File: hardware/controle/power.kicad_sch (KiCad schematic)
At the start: 15 parts, among them J1 Barrel_Jack, U3 TPS54228

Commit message: Adjust some references and availability
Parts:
- C10: P/N C0603C100J5GACTU -> C0603C100J5ACTU
- C9: footprint Capacitor_SMD:C_0805_2012Metric_Pad1.18x1.45mm_HandSolder -> Capacitor_SMD:C_0603_1608Metric_Pad1.08x0.95mm_HandSolder; P/N GRM21BR71E105KA99L -> CGA3E1X7R1V105K080AC (stock)
- R3: footprint Resistor_SMD:R_1206_3216Metric_Pad1.30x1.75mm_HandSolder -> Resistor_SMD:R_0805_2012Metric_Pad1.20x1.40mm_HandSolder; P/N (none) -> stock
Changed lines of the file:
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@@
 			)
 		)
-		(property "Footprint" "Capacitor_SMD:C_0805_2012Metric_Pad1.18x1.45mm_HandSolder"
+		(property "Footprint" "Capacitor_SMD:C_0603_1608Metric_Pad1.08x0.95mm_HandSolder"
 			(at 92.71 92.71 0)
 			(effects
@@
 			)
 		)
-		(property "P/N" "GRM21BR71E105KA99L"
+		(property "P/N" "CGA3E1X7R1V105K080AC (stock)"
 			(at 92.71 92.71 0)
 			(effects
@@
 			)
 		)
-		(property "Footprint" "Resistor_SMD:R_1206_3216Metric_Pad1.30x1.75mm_HandSolder"
+		(property "Footprint" "Resistor_SMD:R_0805_2012Metric_Pad1.20x1.40mm_HandSolder"
 			(at 92.71 71.12 0)
 			(effects
@@
 		(property "Description" ""
 			(at 92.71 71.12 0)
+			(effects
+				(font
+					(size 1.27 1.27)
+				)
+				(hide yes)
+			)
+		)
+		(property "P/N" "stock"
+			(at 92.71 71.12 90)
 			(effects
 				(font
@@
 			)
 		)
-		(property "P/N" "C0603C100J5GACTU"
+		(property "P/N" "C0603C100J5ACTU"
 			(at 148.59 92.71 0)
 			(effects

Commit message: controle: - pass ERC - adjust some components and connections - place components on board
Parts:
- +5V1: symbol centrale-rescue:Conn_01x02_Male-Connector -> Connector_Generic:Conn_01x02
- L1: symbol centrale-rescue:INDUCTOR-pspice -> Device:L_Small
- R5: footprint Resistor_SMD:R_1206_3216Metric_Pad1.30x1.75mm_HandSolder -> Resistor_SMD:R_0805_2012Metric_Pad1.20x1.40mm_HandSolder
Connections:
- net GND: now also J1.3
- no-connect marks 2 -> 0
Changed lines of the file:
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@@
+	)
+	(junction
+		(at 58.42 67.31)
+		(diameter 0)
+		(color 0 0 0 0)
 	)
 	(junction
@@
 		(color 0 0 0 0)
 	)
-	(no_connect
-		(at 194.31 161.29)
-	)
-	(no_connect
-		(at 58.42 64.77)
-	)
 	(wire
 		(pts
@@
 	(wire
 		(pts
-			(xy 149.86 82.55) (xy 152.4 82.55)
+			(xy 149.86 82.55) (xy 156.21 82.55)
 		)
 		(stroke
@@
 	(wire
 		(pts
+			(xy 161.29 82.55) (xy 166.37 82.55)
+		)
+		(stroke
+			(width 0)
+			(type default)
+		)
+	)
+	(wire
+		(pts
 			(xy 118.11 100.33) (xy 118.11 102.87)
 		)
@@
 	(wire
 		(pts
+			(xy 58.42 64.77) (xy 58.42 67.31)
+		)
+		(stroke
+			(width 0)
+			(type default)
+		)
+	)
+	(wire
+		(pts
 			(xy 179.07 100.33) (xy 179.07 95.25)
 		)
@@
 		(pts
 			(xy 68.58 100.33) (xy 68.58 102.87)
-		)
-		(stroke
-			(width 0)
-			(type default)
-		)
-	)
-	(wire
-		(pts
-			(xy 166.37 82.55) (xy 165.1 82.55)
 		)
 		(stroke
@@
 			)
 		)
-		(property "Description" ""
+		(property "Description" "Switching Regulator"
 			(at 118.11 82.55 0)
 			(effects
@@
 			)
 		)
-		(property "Footprint" "Resistor_SMD:R_1206_3216Metric_Pad1.30x1.75mm_HandSolder"
+		(property "Footprint" "Resistor_SMD:R_0805_2012Metric_Pad1.20x1.40mm_HandSolder"
 			(at 144.78 96.52 0)
 			(effects
@@
 	)
 	(symbol
-		(lib_id "centrale-rescue:INDUCTOR-pspice")
-		(at 158.75 82.55 0)
+		(lib_id "Device:L_Small")
+		(at 158.75 82.55 90)
 		(unit 1)
 		(exclude_from_sim no)
@@
 		(dnp no)
 		(property "Reference" "L1"
-			(at 158.75 78.74 0)
+			(at 158.75 80.264 90)
 			(effects
 				(font
@@
 		)
 		(property "Value" "4.7µH"
-			(at 158.75 83.82 0)
+			(at 159.004 84.582 90)
 			(effects
 				(font
@@
 			)
 		)
-		(property "Datasheet" ""
+		(property "Datasheet" "~"
 			(at 158.75 82.55 0)
 			(effects
@@
 					(size 1.27 1.27)
 				)
-			)
-		)
-		(property "Description" ""
+				(hide yes)
+			)
+		)
+		(property "Description" "Inductor, small symbol"
 			(at 158.75 82.55 0)
 			(effects
@@
 	)
 	(symbol
-		(lib_id "centrale-rescue:GND2-power")
+		(lib_id "power:GND")
 		(at 118.11 102.87 0)
 		(unit 1)
@@
 			)
 		)
-		(property "Description" ""
+		(property "Description" "Power symbol creates a global label with name \"GND\" , ground"
 			(at 118.11 102.87 0)
 			(effects
@@
 	)
 	(symbol
-		(lib_id "centrale-rescue:GND2-power")
+		(lib_id "power:GND")
 		(at 130.81 64.77 90)
 		(unit 1)
@@
 			)
 		)
-		(property "Description" ""
+		(property "Description" "Power symbol creates a global label with name \"GND\" , ground"
 			(at 130.81 64.77 0)
 			(effects
@@
 	)
 	(symbol
-		(lib_id "centrale-rescue:Conn_01x02_Male-Connector")
-		(at 189.23 90.17 180)
+		(lib_id "Connector_Generic:Conn_01x02")
+		(at 189.23 90.17 0)
+		(mirror x)
 		(unit 1)
 		(exclude_from_sim no)
@@
 		)
 		(property "Value" "5V_LIME2"
-			(at 190.5 96.52 0)
+			(at 189.23 84.074 0)
 			(effects
 				(font
@@
 			)
 		)
-		(property "Datasheet" ""
+		(property "Datasheet" "~"
 			(at 189.23 90.17 0)
 			(effects
@@
 					(size 1.27 1.27)
 				)
-			)
-		)
-		(property "Description" ""
+				(hide yes)
+			)
+		)
+		(property "Description" "Generic connector, single row, 01x02, script generated (kicad-library-utils/schlib/autogen/connector/)"
 			(at 189.23 90.17 0)
 			(effects
@@
 	)
 	(symbol
-		(lib_id "centrale-rescue:+12V-power")
+		(lib_id "power:+12V")
 		(at 118.11 50.8 0)
 		(unit 1)
@@
 			)
 		)
-		(property "Description" ""
+		(property "Description" "Power symbol creates a global label with name \"+12V\""
 			(at 118.11 50.8 0)
 			(effects
+				(font
+					(size 1.27 1.27)
+				)
+				(hide yes)
+			)
+		)
+		(property "P/N" ""
+			(at 118.11 50.8 0)
+			(effects

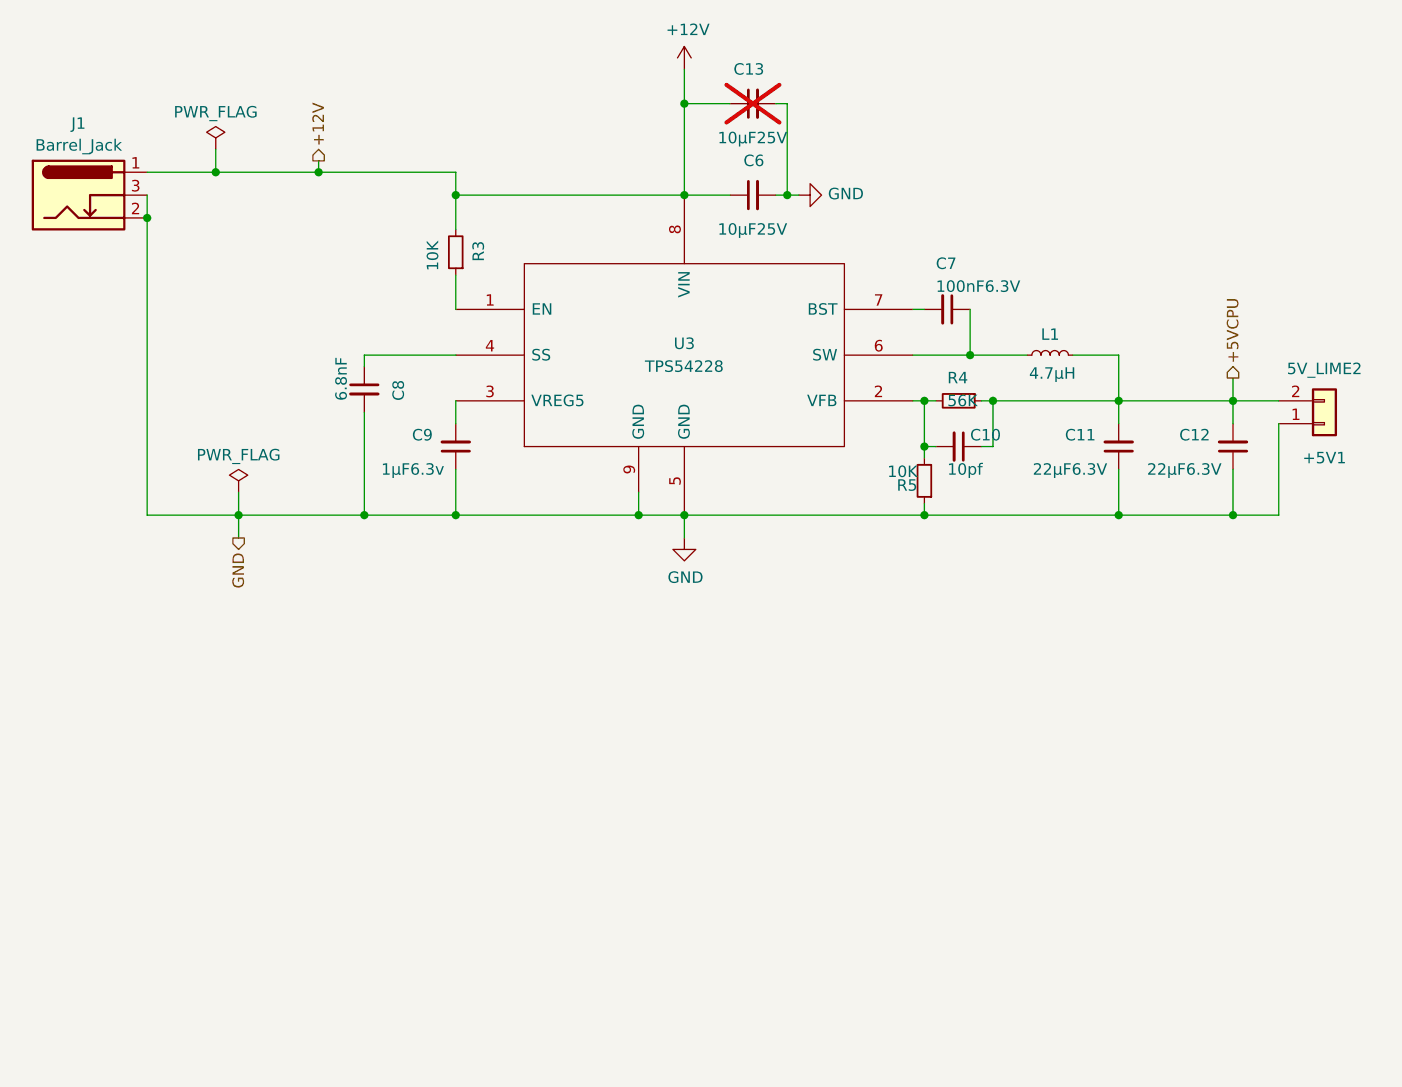
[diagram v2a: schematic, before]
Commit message: hardware/controle: control CPU power from pic18: - add a separate 3.3V power for pic18 - use the pic18 to start the tps54228
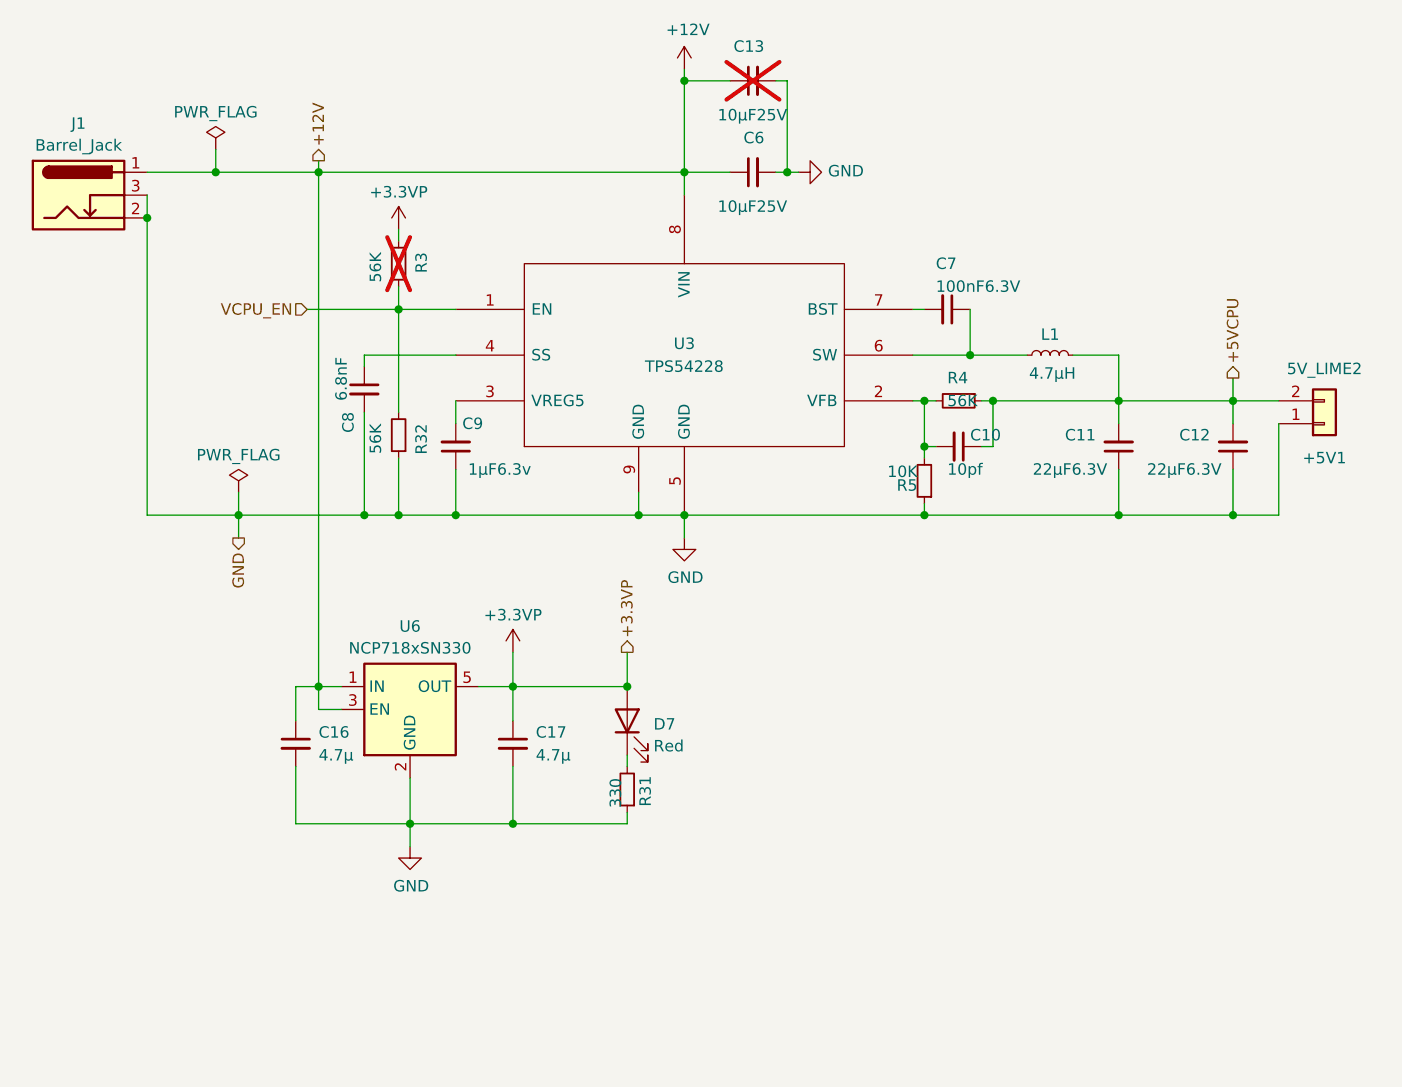
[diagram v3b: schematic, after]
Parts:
- added C16, C17: 4.7µ, Capacitor_SMD:C_0805_2012Metric_Pad1.18x1.45mm_HandSolder, symbol Device:C_Small
- added D7: Red, LED_SMD:LED_0805_2012Metric, symbol Device:LED
- added R31: 330, Resistor_SMD:R_0805_2012Metric_Pad1.20x1.40mm_HandSolder, symbol Device:R_Small
- added R32: 56K, Resistor_SMD:R_0805_2012Metric_Pad1.20x1.40mm_HandSolder, symbol Device:R_Small
- added U6: NCP718xSN330, Package_TO_SOT_SMD:SOT-23-5, symbol Regulator_Linear:NCP718xSN330
- R3: value 10K -> 56K; now not fitted; now left out of the parts list
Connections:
- net +12V: now also C16.1, U6.1 (IN), U6.3 (EN); no longer R3.2
- net GND: now also C16.2, C17.2, R31.1, R32.1, U6.2 (GND)
- net VCPU_EN: now reaches R3.1, U3.1 (EN)
- net VCPU_EN: now also R32.2
- new net: D7.1 (K), R31.2
- new net +3.3VP: C17.1, D7.2 (A), R3.2, U6.5 (OUT)
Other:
- moved on the sheet: C13, C6

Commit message: hardware/controle: route control CPU power from pic18
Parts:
- renumbered C9 to C10, C10 to C11, C11 to C12, C12 to C13, C16 to C14, C17 to C15, C13 to C6, C6 to C7, C7 to C8, C8 to C9, J1 to J9, R3 to R24, R4 to R25, R32 to R26, R5 to R27, R31 to R28, U3 to U4, U6 to U5
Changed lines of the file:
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@@
 		(on_board yes)
 		(dnp no)
-		(property "Reference" "#PWR022"
+		(property "Reference" "#PWR025"
 			(at 87.63 143.51 0)
 			(effects
@@
 			(project "controle"
 				(path "/41099c3f-2f7d-470d-b75f-9309d43eb2d2/523a32f9-902b-415b-ba1d-6227a5ae26a9"
-					(reference "#PWR022")
+					(reference "#PWR025")
 					(unit 1)
 				)
@@
 		(dnp no)
 		(fields_autoplaced yes)
-		(property "Reference" "#PWR01"
+		(property "Reference" "#PWR024"
 			(at 102.87 116.84 0)
 			(effects
@@
 			(project "controle"
 				(path "/41099c3f-2f7d-470d-b75f-9309d43eb2d2/523a32f9-902b-415b-ba1d-6227a5ae26a9"
-					(reference "#PWR01")
+					(reference "#PWR024")
 					(unit 1)
 				)
@@
 		(on_board yes)
 		(dnp no)
-		(property "Reference" "C9"
+		(property "Reference" "C10"
 			(at 95.758 90.17 0)
 			(effects
@@
 			(project "controle"
 				(path "/41099c3f-2f7d-470d-b75f-9309d43eb2d2/523a32f9-902b-415b-ba1d-6227a5ae26a9"
-					(reference "C9")
+					(reference "C10")
 					(unit 1)
 				)
@@
 		(on_board yes)
 		(dnp no)
-		(property "Reference" "C7"
+		(property "Reference" "C8"
 			(at 146.05 72.39 90)
 			(effects
@@
 			(project "controle"
 				(path "/41099c3f-2f7d-470d-b75f-9309d43eb2d2/523a32f9-902b-415b-ba1d-6227a5ae26a9"
-					(reference "C7")
+					(reference "C8")
 					(unit 1)
 				)
@@
 		(on_board yes)
 		(dnp yes)
-		(property "Reference" "C13"
+		(property "Reference" "C6"
 			(at 127 48.26 90)
 			(effects
@@
 			(project "controle"
 				(path "/41099c3f-2f7d-470d-b75f-9309d43eb2d2/523a32f9-902b-415b-ba1d-6227a5ae26a9"
-					(reference "C13")
+					(reference "C6")
 					(unit 1)
 				)
@@
 		(on_board yes)
 		(dnp no)
-		(property "Reference" "R4"
+		(property "Reference" "R25"
 			(at 147.32 85.09 90)
 			(effects
@@
 			(project "controle"
 				(path "/41099c3f-2f7d-470d-b75f-9309d43eb2d2/523a32f9-902b-415b-ba1d-6227a5ae26a9"
-					(reference "R4")
+					(reference "R25")
 					(unit 1)
 				)
@@
 		(on_board yes)
 		(dnp no)
-		(property "Reference" "C6"
+		(property "Reference" "C7"
 			(at 127 58.42 90)
 			(effects
@@
 			(project "controle"
 				(path "/41099c3f-2f7d-470d-b75f-9309d43eb2d2/523a32f9-902b-415b-ba1d-6227a5ae26a9"
-					(reference "C6")
+					(reference "C7")
 					(unit 1)
 				)
@@
 		(on_board yes)
 		(dnp no)
-		(property "Reference" "U3"
+		(property "Reference" "U4"
 			(at 118.11 81.28 0)
 			(effects
@@
 			(project "controle"
 				(path "/41099c3f-2f7d-470d-b75f-9309d43eb2d2/523a32f9-902b-415b-ba1d-6227a5ae26a9"
-					(reference "U3")
+					(reference "U4")
 					(unit 1)
 				)
@@
 		(on_board yes)
 		(dnp no)
-		(property "Reference" "R5"
+		(property "Reference" "R27"
 			(at 144.018 97.028 0)
 			(effects
@@
 			(project "controle"
 				(path "/41099c3f-2f7d-470d-b75f-9309d43eb2d2/523a32f9-902b-415b-ba1d-6227a5ae26a9"
-					(reference "R5")
+					(reference "R27")
 					(unit 1)
 				)
@@
 		(on_board yes)
 		(dnp no)
-		(property "Reference" "C12"
+		(property "Reference" "C13"
 			(at 176.53 91.44 0)
 			(effects
@@
 			(project "controle"
 				(path "/41099c3f-2f7d-470d-b75f-9309d43eb2d2/523a32f9-902b-415b-ba1d-6227a5ae26a9"
-					(reference "C12")
+					(reference "C13")
 					(unit 1)
 				)
@@
 		(dnp no)
 		(fields_autoplaced yes)
-		(property "Reference" "U6"
+		(property "Reference" "U5"
 			(at 87.63 112.6955 0)
 			(effects
@@
 			(project "controle"
 				(path "/41099c3f-2f7d-470d-b75f-9309d43eb2d2/523a32f9-902b-415b-ba1d-6227a5ae26a9"
-					(reference "U6")
+					(reference "U5")
 					(unit 1)
 				)
@@
 		(dnp no)
 		(fields_autoplaced yes)
-		(property "Reference" "#PWR035"
+		(property "Reference" "#PWR022"
 			(at 90.17 69.85 0)
 			(effects
@@
 			(project "controle"
 				(path "/41099c3f-2f7d-470d-b75f-9309d43eb2d2/523a32f9-902b-415b-ba1d-6227a5ae26a9"
-					(reference "#PWR035")
+					(reference "#PWR022")
 					(unit 1)
 				)
@@
 		(dnp no)
 		(fields_autoplaced yes)
-		(property "Reference" "C16"
+		(property "Reference" "C14"
 			(at 77.47 124.4662 0)
 			(effects
@@
 			(project "controle"
 				(path "/41099c3f-2f7d-470d-b75f-9309d43eb2d2/523a32f9-902b-415b-ba1d-6227a5ae26a9"
-					(reference "C16")
+					(reference "C14")
 					(unit 1)
 				)
@@
 		(on_board yes)
 		(dnp yes)
-		(property "Reference" "R3"
+		(property "Reference" "R24"
 			(at 88.9 71.12 90)
 			(effects
@@
 			(project "controle"
 				(path "/41099c3f-2f7d-470d-b75f-9309d43eb2d2/523a32f9-902b-415b-ba1d-6227a5ae26a9"
-					(reference "R3")
+					(reference "R24")
 					(unit 1)
 				)
@@
 		(on_board yes)
 		(dnp no)
-		(property "Reference" "#PWR09"
+		(property "Reference" "#PWR023"
 			(at 118.11 109.22 0)
 			(effects
@@
 			(project "controle"
 				(path "/41099c3f-2f7d-470d-b75f-9309d43eb2d2/523a32f9-902b-415b-ba1d-6227a5ae26a9"
-					(reference "#PWR09")
+					(reference "#PWR023")
 					(unit 1)
 				)
@@
 		(on_board yes)
 		(dnp no)
-		(property "Reference" "R32"
+		(property "Reference" "R26"
 			(at 88.9 90.17 90)
 			(effects
@@
 			(project "controle"
 				(path "/41099c3f-2f7d-470d-b75f-9309d43eb2d2/523a32f9-902b-415b-ba1d-6227a5ae26a9"
-					(reference "R32")
+					(reference "R26")
 					(unit 1)
 				)
@@
 		(dnp no)
 		(fields_autoplaced yes)
-		(property "Reference" "C17"
+		(property "Reference" "C15"
 			(at 101.6 124.4662 0)
 			(effects
@@
 			(project "controle"
 				(path "/41099c3f-2f7d-470d-b75f-9309d43eb2d2/523a32f9-902b-415b-ba1d-6227a5ae26a9"
-					(reference "C17")
+					(reference "C15")
 					(unit 1)
 				)
@@
 		(on_board yes)
 		(dnp no)
-		(property "Reference" "C8"
+		(property "Reference" "C9"
 			(at 80.772 91.186 90)
 			(effects
@@
 			(project "controle"
 				(path "/41099c3f-2f7d-470d-b75f-9309d43eb2d2/523a32f9-902b-415b-ba1d-6227a5ae26a9"
-					(reference "C8")
+					(reference "C9")
 					(unit 1)
 				)
@@
 		(on_board yes)
 		(dnp no)
-		(property "Reference" "R31"
+		(property "Reference" "R28"
 			(at 113.792 129.286 90)
 			(effects
@@
 			(project "controle"
 				(path "/41099c3f-2f7d-470d-b75f-9309d43eb2d2/523a32f9-902b-415b-ba1d-6227a5ae26a9"
-					(reference "R31")
+					(reference "R28")
 					(unit 1)
 				)
@@
 		(dnp no)
 		(fields_autoplaced yes)
-		(property "Reference" "#FLG01"
+		(property "Reference" "#FLG03"
 			(at 66.04 57.785 0)
 			(effects
@@
 			(project "controle"
 				(path "/41099c3f-2f7d-470d-b75f-9309d43eb2d2/523a32f9-902b-415b-ba1d-6227a5ae26a9"
-					(reference "#FLG01")
+					(reference "#FLG03")
 					(unit 1)
 				)
@@
 		(on_board yes)
 		(dnp no)
-		(property "Reference" "#PWR08"
+		(property "Reference" "#PWR021"
 			(at 137.16 62.23 0)
 			(effects
@@
 			(project "controle"
 				(path "/41099c3f-2f7d-470d-b75f-9309d43eb2d2/523a32f9-902b-415b-ba1d-6227a5ae26a9"
-					(reference "#PWR08")
+					(reference "#PWR021")
 					(unit 1)
 				)
@@
 		(dnp no)
 		(fields_autoplaced yes)
-		(property "Reference" "J1"
+		(property "Reference" "J9"
 			(at 50.8 56.8155 0)
 			(effects
@@
 			(project "controle"
 				(path "/41099c3f-2f7d-470d-b75f-9309d43eb2d2/523a32f9-902b-415b-ba1d-6227a5ae26a9"
-					(reference "J1")
+					(reference "J9")
 					(unit 1)
 				)
@@
 		(on_board yes)
 		(dnp no)
-		(property "Reference" "C11"
+		(property "Reference" "C12"
 			(at 163.83 91.44 0)
 			(effects
@@
 			(project "controle"
 				(path "/41099c3f-2f7d-470d-b75f-9309d43eb2d2/523a32f9-902b-415b-ba1d-6227a5ae26a9"
-					(reference "C11")
+					(reference "C12")
 					(unit 1)
 				)
@@
 		(dnp no)
 		(fields_autoplaced yes)
-		(property "Reference" "#FLG02"
+		(property "Reference" "#FLG04"
 			(at 68.58 95.885 0)
 			(effects
@@
 			(project "controle"
 				(path "/41099c3f-2f7d-470d-b75f-9309d43eb2d2/523a32f9-902b-415b-ba1d-6227a5ae26a9"
-					(reference "#FLG02")
+					(reference "#FLG04")
 					(unit 1)
 				)
@@
 		(on_board yes)
 		(dnp no)
-		(property "Reference" "#PWR07"
+		(property "Reference" "#PWR020"
 			(at 118.11 54.61 0)
 			(effects
@@
 			(project "controle"
 				(path "/41099c3f-2f7d-470d-b75f-9309d43eb2d2/523a32f9-902b-415b-ba1d-6227a5ae26a9"
-					(reference "#PWR07")
+					(reference "#PWR020")
 					(unit 1)
 				)
@@
 		(on_board yes)
 		(dnp no)
-		(property "Reference" "C10"
+		(property "Reference" "C11"
 			(at 149.86 91.44 90)
 			(effects
@@
 			(project "controle"
 				(path "/41099c3f-2f7d-470d-b75f-9309d43eb2d2/523a32f9-902b-415b-ba1d-6227a5ae26a9"
-					(reference "C10")
-					(unit 1)
-				)
+					(reference "C11")
+					(unit 1)
+				)
